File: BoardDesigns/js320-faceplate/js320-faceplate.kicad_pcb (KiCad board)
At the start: 2 copper layers, 95 x 24.7 mm, 20 parts, among them J1 JS220, J3 Conn_01x04_Socket, J4 54-00286, SW1 SS-10-23NPE, U1 LT3045xDD, U2 XC6206PxxxMR, U4 PUCC33420RAQR

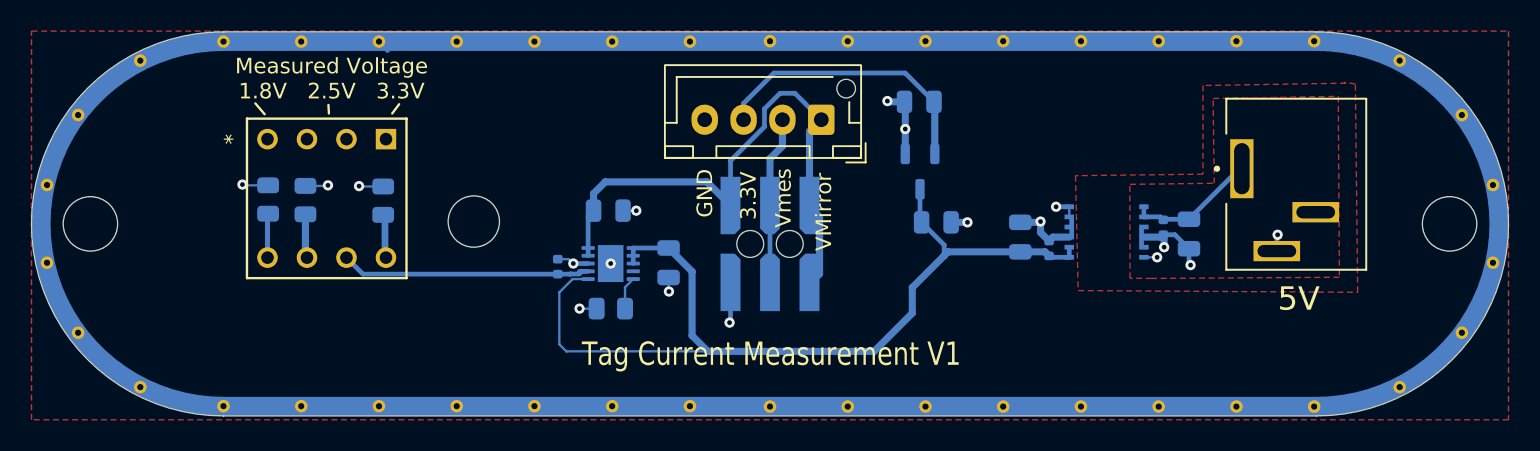
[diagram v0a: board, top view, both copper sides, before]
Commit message: update js320 with Matt Liberty's comments
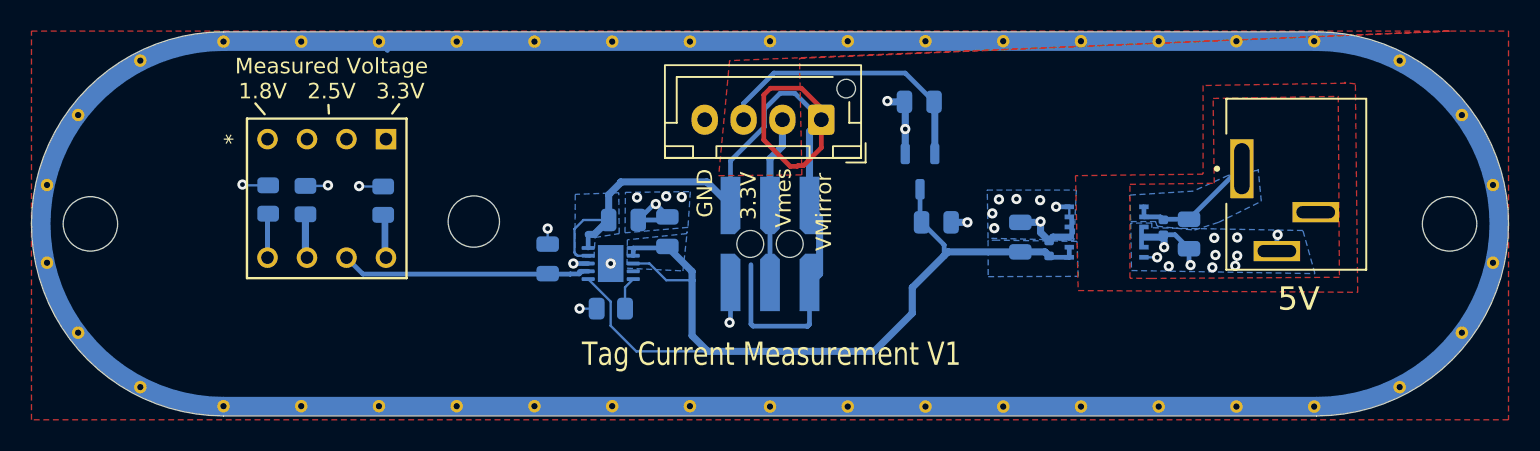
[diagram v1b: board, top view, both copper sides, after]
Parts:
- C2: value 22nf -> 470nf; footprint Capacitor_SMD:C_0402_1005Metric -> Capacitor_SMD:C_0805_2012Metric
- moved C1 2.00 mm to (131.9, 80.4), turned to 90 degrees
- moved C3 1.14 mm to (129.1, 79.7)
- moved C2 0.82 mm to (124.2, 82.2)
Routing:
- net /Vprog: track 37.6 -> 66.6 mm
- net GND: track 23.7 -> 26.2 mm, vias 14 -> 22
- net /vin: track 58.9 -> 57.8 mm
- net GNDPWR: vias 4 -> 11
- added copper zone on B.Cu, net /VINP
- added copper zone on B.Cu, net /Vprog
- added copper zone on B.Cu, net /vin
- added copper zone on B.Cu, net GND
- added copper zone on B.Cu, net GNDPWR
